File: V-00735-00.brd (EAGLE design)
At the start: 41 x 73 mm, 32 parts, among them IC2 MAX481CSA, IC3 FT232RL, IC8 ATMEGA644A, Q1 14.7456MHz, X1 MINI-USB-SCHIELD-32005-201

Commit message: v1.1.0.2
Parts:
- IC8: value ATMEGA644A -> ATMEGA644P
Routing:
- net GND: track 27.5 -> 42.8 mm
- net +5V: track 176.7 -> 188.2 mm
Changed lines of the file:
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@@
 <layer number="14" name="Route14" color="1" fill="6" visible="no" active="yes"/>
 <layer number="15" name="Route15" color="4" fill="6" visible="no" active="yes"/>
-<layer number="16" name="Bottom" color="4" fill="1" visible="no" active="yes"/>
+<layer number="16" name="Bottom" color="4" fill="1" visible="yes" active="yes"/>
 <layer number="17" name="Pads" color="2" fill="1" visible="yes" active="yes"/>
 <layer number="18" name="Vias" color="2" fill="1" visible="yes" active="yes"/>
-<layer number="19" name="Unrouted" color="6" fill="1" visible="no" active="yes"/>
+<layer number="19" name="Unrouted" color="6" fill="1" visible="yes" active="yes"/>
 <layer number="20" name="Dimension" color="15" fill="1" visible="yes" active="yes"/>
-<layer number="21" name="tPlace" color="7" fill="1" visible="no" active="yes"/>
-<layer number="22" name="bPlace" color="7" fill="1" visible="no" active="yes"/>
-<layer number="23" name="tOrigins" color="15" fill="1" visible="no" active="yes"/>
-<layer number="24" name="bOrigins" color="15" fill="1" visible="no" active="yes"/>
-<layer number="25" name="tNames" color="7" fill="1" visible="no" active="yes"/>
-<layer number="26" name="bNames" color="7" fill="1" visible="no" active="yes"/>
-<layer number="27" name="tValues" color="7" fill="1" visible="no" active="yes"/>
-<layer number="28" name="bValues" color="7" fill="1" visible="no" active="yes"/>
+<layer number="21" name="tPlace" color="7" fill="1" visible="yes" active="yes"/>
+<layer number="22" name="bPlace" color="7" fill="1" visible="yes" active="yes"/>
+<layer number="23" name="tOrigins" color="15" fill="1" visible="yes" active="yes"/>
+<layer number="24" name="bOrigins" color="15" fill="1" visible="yes" active="yes"/>
+<layer number="25" name="tNames" color="7" fill="1" visible="yes" active="yes"/>
+<layer number="26" name="bNames" color="7" fill="1" visible="yes" active="yes"/>
+<layer number="27" name="tValues" color="7" fill="1" visible="yes" active="yes"/>
+<layer number="28" name="bValues" color="7" fill="1" visible="yes" active="yes"/>
 <layer number="29" name="tStop" color="7" fill="3" visible="no" active="yes"/>
 <layer number="30" name="bStop" color="7" fill="6" visible="no" active="yes"/>
@@
 <element name="D4" library="#PaJa_31" package="P1206" value="OSTG1206C1A_N" x="18.3" y="64.3"/>
 <element name="R15" library="#PaJa_31" package="1206" value="580R" x="23.7" y="64.3" rot="R180"/>
-<element name="IC8" library="atmel" package="TQFP44" value="ATMEGA644A" x="16.2" y="38.1" rot="MR0">
-<attribute name="OC_NEWARK" value="58M3748" x="16.2" y="38.1" size="1.778" layer="28" rot="MR0" display="off"/>
-<attribute name="MPN" value="ATMEGA644PV-10AU" x="16.2" y="38.1" size="1.778" layer="28" rot="MR0" display="off"/>
-<attribute name="MF" value="" x="16.2" y="38.1" size="1.778" layer="28" rot="MR0" display="off"/>
-<attribute name="OC_FARNELL" value="1455123" x="16.2" y="38.1" size="1.778" layer="28" rot="MR0" display="off"/>
-</element>
+<element name="IC8" library="atmel" package="TQFP44" value="ATMEGA644P" x="16.2" y="38.1" rot="MR0"/>
 <element name="JUM1" library="#PaJa_konektory" package="S1G3_JUM" value="S1G3_JUMP" x="2.7" y="36.7" rot="R90"/>
 <element name="JUM2" library="#PaJa_konektory" package="S1G4_JUM" value="S1G4_JUMP" x="2.7" y="45.6" rot="R90"/>
@@
 <contactref element="IC3" pad="7"/>
 <contactref element="R15" pad="1"/>
+<contactref element="IC8" pad="39"/>
 <contactref element="IC8" pad="6"/>
-<contactref element="IC8" pad="39"/>
+<contactref element="IC8" pad="18"/>
 <contactref element="IC8" pad="28"/>
-<contactref element="IC8" pad="18"/>
 <contactref element="JUM1" pad="3"/>
 <contactref element="K1" pad="4"/>
@@
 <via x="5.2" y="26" extent="1-16" drill="0.6"/>
 <wire x1="10.4" y1="38.1" x2="7.9" y2="38.1" width="0.4064" layer="16"/>
-<wire x1="16.2" y1="43.9" x2="16.2" y2="45.1" width="0.4064" layer="16"/>
+<wire x1="22" y1="38.1" x2="16.2" y2="45.1" width="0.4064" layer="16"/>
 <wire x1="16.2" y1="45.1" x2="16.3" y2="45.2" width="0.4064" layer="16"/>
-<wire x1="15.4" y1="32.3" x2="15.4" y2="31" width="0.4064" layer="16"/>
+<wire x1="10.4" y1="38.1" x2="15.4" y2="31" width="0.4064" layer="16"/>
 <wire x1="15.4" y1="31" x2="15" y2="30.6" width="0.4064" layer="16"/>
 <wire x1="27.925" y1="18.175" x2="27.925" y2="19.375" width="0.4064" layer="16"/>
@@
 <wire x1="29.875" y1="18.175" x2="29.875" y2="15.025" width="0.4064" layer="16"/>
 <wire x1="29.875" y1="15.025" x2="30.7" y2="14.2" width="0.4064" layer="16"/>
+<wire x1="16.2" y1="45.1" x2="16.2" y2="43.9" width="0" layer="19" extent="16-16"/>
+<wire x1="15.4" y1="32.3" x2="15.4" y2="31" width="0" layer="19" extent="16-16"/>
 </signal>
 <signal name="RS485_EN">
@@
 <contactref element="C5" pad="2"/>
 <contactref element="U$1" pad="4"/>
+<contactref element="IC8" pad="5"/>
 <contactref element="IC8" pad="38"/>
-<contactref element="IC8" pad="5"/>
 <contactref element="IC8" pad="17"/>
 <contactref element="JUM1" pad="1"/>
@@
 <vertex x="12.2" y="34.4"/>
 </polygon>
-<wire x1="22" y1="38.9" x2="19.3" y2="38.9" width="0.4064" layer="16"/>
+<wire x1="15.4" y1="43.9" x2="19.3" y2="38.9" width="0.4064" layer="16"/>
 <wire x1="19.3" y1="38.9" x2="19" y2="39.2" width="0.4064" layer="16"/>
 <wire x1="17.3925" y1="56.58" x2="17.3925" y2="58.395" width="0.4064" layer="1"/>
@@
 <wire x1="26.63" y1="53.27" x2="23.32" y2="56.58" width="0.4064" layer="1"/>
 <wire x1="17.3925" y1="56.58" x2="23.32" y2="56.58" width="0.4064" layer="1"/>
-<wire x1="22" y1="38.9" x2="24.7" y2="38.9" width="0.4064" layer="16"/>
+<wire x1="15.4" y1="43.9" x2="24.7" y2="38.9" width="0.4064" layer="16"/>
 <wire x1="24.7" y1="38.9" x2="27" y2="41.2" width="0.4064" layer="16"/>
 <wire x1="27" y1="41.2" x2="30" y2="41.2" width="0.4064" layer="16"/>
@@
 <wire x1="27.4" y1="18.4" x2="27.4" y2="20.2125" width="0.4064" layer="1"/>
 <wire x1="10.2875" y1="20.2125" x2="11.5" y2="20.2125" width="0.4064" layer="1"/>
+<wire x1="24.7" y1="38.9" x2="22" y2="38.9" width="0" layer="19" extent="16-16"/>
 </signal>
 <signal name="AREF">

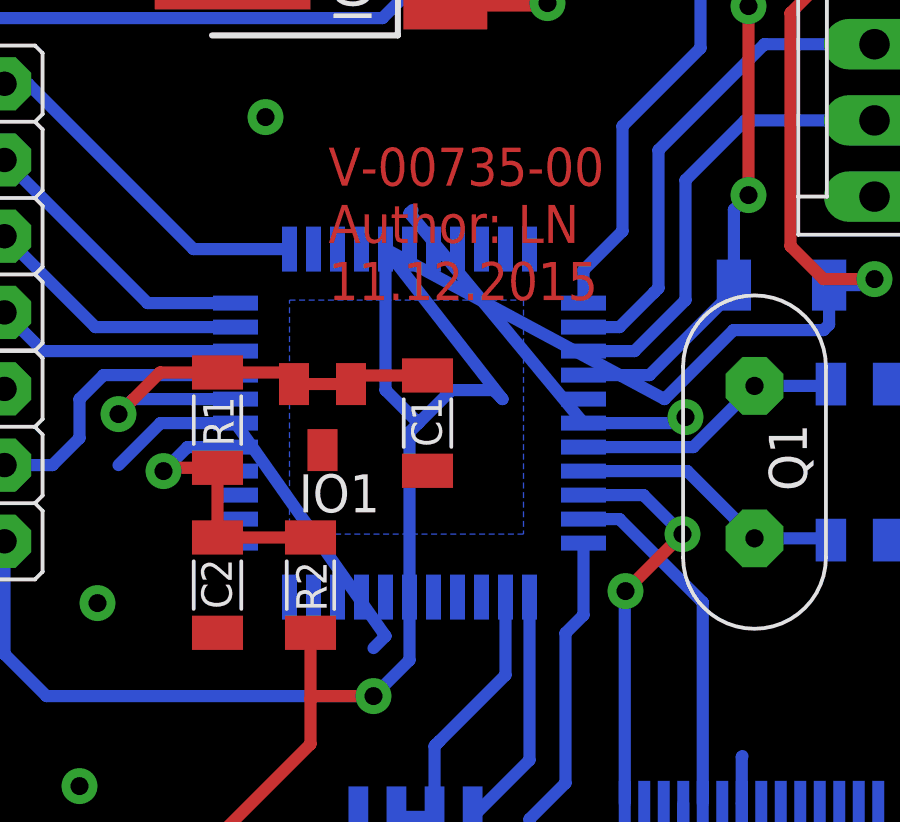
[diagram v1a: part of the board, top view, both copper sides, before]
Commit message: v1.1.0.3
Opraveny spoje, nevím proč ale byli divně pospojované. Ale plošnák OK.
ALe nastal problém v stabilizátoru. Blbec jsem si nevšiml vstupního
napájení které pro použitej stabilizátor je pouze 16V proto je nutné ho
nahradit například 78L05-TO92
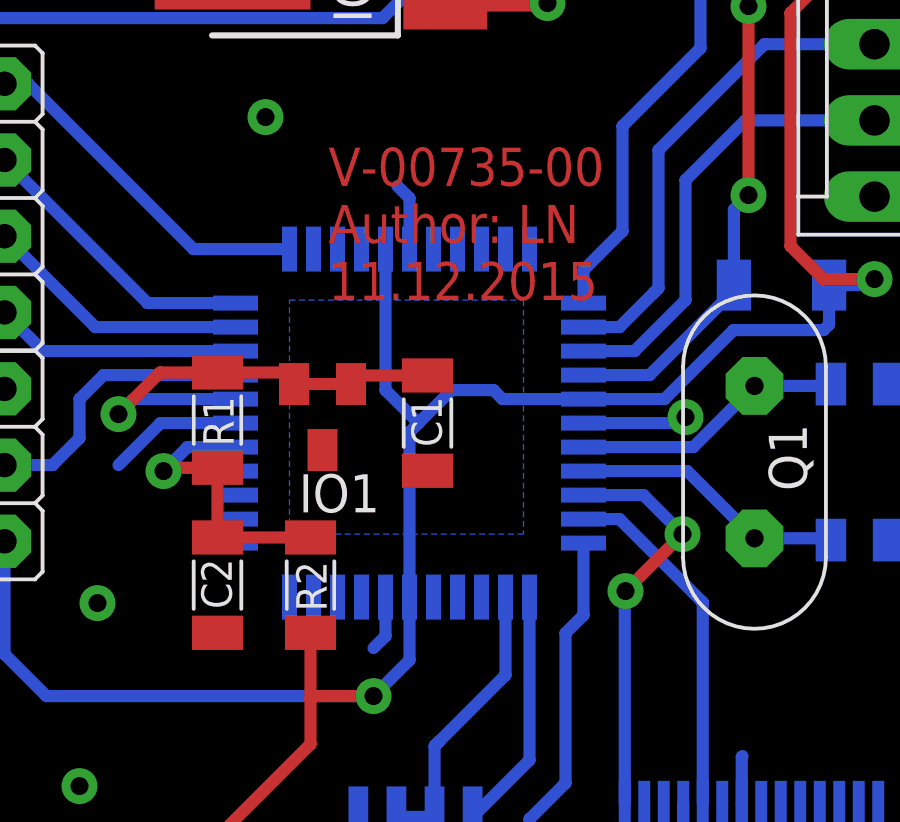
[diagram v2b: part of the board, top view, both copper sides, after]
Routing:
- net GND: track 42.8 -> 28.5 mm
- net +5V: track 188.2 -> 176.7 mm
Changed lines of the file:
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@@
 <grid distance="0.1" unitdist="mm" unit="mm" style="lines" multiple="2" display="yes" altdistance="0.05" altunitdist="mm" altunit="mm"/>
 <layers>
-<layer number="1" name="Top" color="3" fill="1" visible="yes" active="yes"/>
+<layer number="1" name="Top" color="3" fill="1" visible="no" active="yes"/>
 <layer number="2" name="Route2" color="1" fill="3" visible="no" active="yes"/>
 <layer number="3" name="Route3" color="4" fill="3" visible="no" active="yes"/>
@@
 <layer number="19" name="Unrouted" color="6" fill="1" visible="yes" active="yes"/>
 <layer number="20" name="Dimension" color="15" fill="1" visible="yes" active="yes"/>
-<layer number="21" name="tPlace" color="7" fill="1" visible="yes" active="yes"/>
+<layer number="21" name="tPlace" color="7" fill="1" visible="no" active="yes"/>
 <layer number="22" name="bPlace" color="7" fill="1" visible="yes" active="yes"/>
-<layer number="23" name="tOrigins" color="15" fill="1" visible="yes" active="yes"/>
+<layer number="23" name="tOrigins" color="15" fill="1" visible="no" active="yes"/>
 <layer number="24" name="bOrigins" color="15" fill="1" visible="yes" active="yes"/>
-<layer number="25" name="tNames" color="7" fill="1" visible="yes" active="yes"/>
+<layer number="25" name="tNames" color="7" fill="1" visible="no" active="yes"/>
 <layer number="26" name="bNames" color="7" fill="1" visible="yes" active="yes"/>
-<layer number="27" name="tValues" color="7" fill="1" visible="yes" active="yes"/>
+<layer number="27" name="tValues" color="7" fill="1" visible="no" active="yes"/>
 <layer number="28" name="bValues" color="7" fill="1" visible="yes" active="yes"/>
 <layer number="29" name="tStop" color="7" fill="3" visible="no" active="yes"/>
@@
 <via x="5.2" y="26" extent="1-16" drill="0.6"/>
 <wire x1="10.4" y1="38.1" x2="7.9" y2="38.1" width="0.4064" layer="16"/>
-<wire x1="22" y1="38.1" x2="16.2" y2="45.1" width="0.4064" layer="16"/>
-<wire x1="16.2" y1="45.1" x2="16.3" y2="45.2" width="0.4064" layer="16"/>
-<wire x1="10.4" y1="38.1" x2="15.4" y2="31" width="0.4064" layer="16"/>
 <wire x1="15.4" y1="31" x2="15" y2="30.6" width="0.4064" layer="16"/>
 <wire x1="27.925" y1="18.175" x2="27.925" y2="19.375" width="0.4064" layer="16"/>
@@
 <wire x1="29.875" y1="18.175" x2="29.875" y2="15.025" width="0.4064" layer="16"/>
 <wire x1="29.875" y1="15.025" x2="30.7" y2="14.2" width="0.4064" layer="16"/>
-<wire x1="16.2" y1="45.1" x2="16.2" y2="43.9" width="0" layer="19" extent="16-16"/>
-<wire x1="15.4" y1="32.3" x2="15.4" y2="31" width="0" layer="19" extent="16-16"/>
+<wire x1="16.2" y1="43.9" x2="16.2" y2="45.6" width="0.4064" layer="16"/>
+<wire x1="16.2" y1="45.6" x2="15.8" y2="46" width="0.4064" layer="16"/>
+<wire x1="15.4" y1="32.3" x2="15.4" y2="31" width="0.4064" layer="16"/>
 </signal>
 <signal name="RS485_EN">
@@
 <vertex x="12.2" y="34.4"/>
 </polygon>
-<wire x1="15.4" y1="43.9" x2="19.3" y2="38.9" width="0.4064" layer="16"/>
 <wire x1="19.3" y1="38.9" x2="19" y2="39.2" width="0.4064" layer="16"/>
 <wire x1="17.3925" y1="56.58" x2="17.3925" y2="58.395" width="0.4064" layer="1"/>
@@
 <wire x1="26.63" y1="53.27" x2="23.32" y2="56.58" width="0.4064" layer="1"/>
 <wire x1="17.3925" y1="56.58" x2="23.32" y2="56.58" width="0.4064" layer="1"/>
-<wire x1="15.4" y1="43.9" x2="24.7" y2="38.9" width="0.4064" layer="16"/>
 <wire x1="24.7" y1="38.9" x2="27" y2="41.2" width="0.4064" layer="16"/>
 <wire x1="27" y1="41.2" x2="30" y2="41.2" width="0.4064" layer="16"/>
@@
 <wire x1="27.4" y1="18.4" x2="27.4" y2="20.2125" width="0.4064" layer="1"/>
 <wire x1="10.2875" y1="20.2125" x2="11.5" y2="20.2125" width="0.4064" layer="1"/>
-<wire x1="24.7" y1="38.9" x2="22" y2="38.9" width="0" layer="19" extent="16-16"/>
+<wire x1="24.7" y1="38.9" x2="22" y2="38.9" width="0.4064" layer="16"/>
+<wire x1="19.3" y1="38.9" x2="22" y2="38.9" width="0.4064" layer="16"/>
 </signal>
 <signal name="AREF">
